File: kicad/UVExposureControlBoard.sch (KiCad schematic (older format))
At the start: 68 parts, among them P1 POWER, P2 LED 24V, P3 LED GND, P4 SPY BI WIRE, Q1 PMV20XN, Q2 PMV20XN, U1 MC34063, U2 ENC28J60, U3 08B1-1X1T-06-F, U4 MSP430F5438

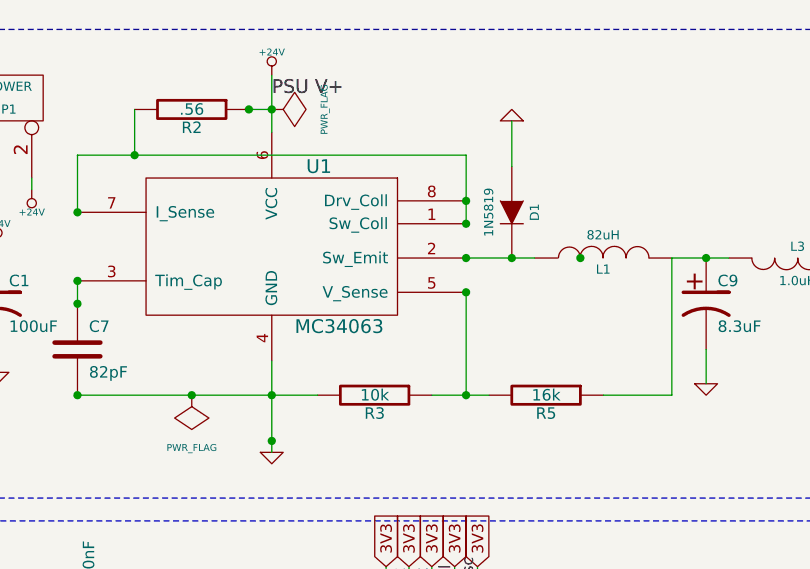
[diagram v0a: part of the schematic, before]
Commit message: PSU components had values that were incorrect (fixed). Silkscreen text on the back was not mirrored (fixed).
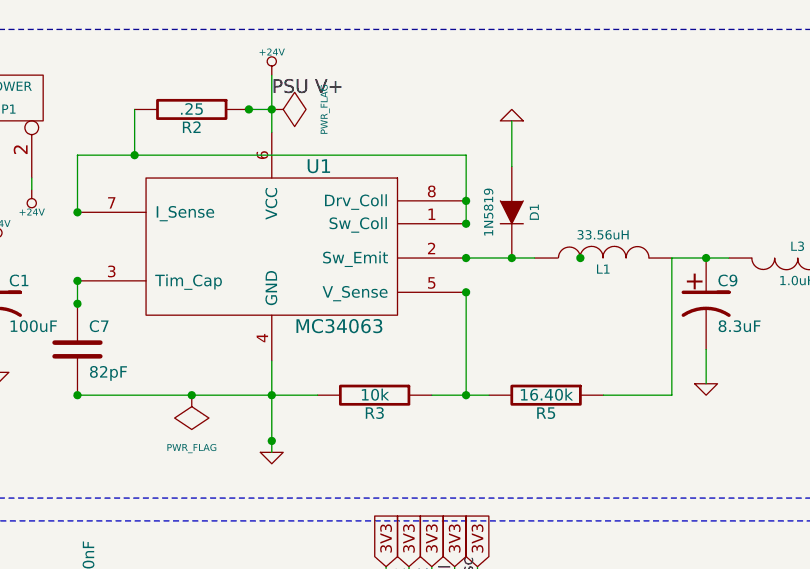
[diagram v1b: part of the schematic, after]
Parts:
- L1: value 82uH -> 33.56uH
- R2: value .56 -> .25
- R5: value 16k -> 16.40k
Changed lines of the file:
@@
-EESchema Schematic File Version 2  date Thu 12 Apr 2012 11:44:37 PM EDT
+EESchema Schematic File Version 2  date Wed 30 Jan 2013 09:46:29 PM EST
 LIBS:power
 LIBS:device
@@
 Sheet 1 1
 Title "UV Exposure Box Control Board"
-Date "13 apr 2012"
+Date "31 jan 2013"
 Rev "1"
 Comp "Jon Neal"
@@
 P 3300 2150
 F 0 "R5" V 3380 2150 50  0000 C CNN
-F 1 "16k" V 3300 2150 50  0000 C CNN
+F 1 "16.40k" V 3300 2150 50  0000 C CNN
 	1    3300 2150
 	0    1    1    0
@@
 P 3550 1550
 F 0 "L1" V 3500 1550 40  0000 C CNN
-F 1 "82uH" V 3650 1550 40  0000 C CNN
+F 1 "33.56uH" V 3650 1550 40  0000 C CNN
 	1    3550 1550
 	0    -1   -1   0
@@
 P 1750 900
 F 0 "R2" V 1830 900 50  0000 C CNN
-F 1 ".56" V 1750 900 50  0000 C CNN
+F 1 ".25" V 1750 900 50  0000 C CNN
 	1    1750 900
 	0    1    1    0
